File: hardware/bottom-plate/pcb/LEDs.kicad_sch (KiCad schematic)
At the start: 96 parts

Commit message: kicker pcb done, working on bottom plate
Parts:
- R100, R101, R102, R103, R104, R105, R106, R107, R108, R109, R110, R111, R112, R113, R114, R115, R68, R69, R70, R71, R72, R73, R74, R75, R76, R77, R78, R79, R80, R81, R82, R83, R84, R85, R86, R87, R88, R89, R90, R91, R92, R93, R94, R95, R96, R97, R98, R99: footprint PCM_Resistor_SMD_AKL:R_0603_1608Metric_Pad0.98x0.95mm_HandSolder -> PCM_Resistor_SMD_AKL:R_0805_2012Metric_Pad1.15x1.40mm_HandSolder

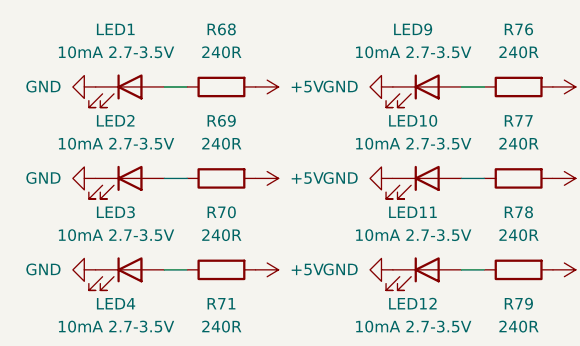
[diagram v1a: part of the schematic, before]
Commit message: cleaned up bottom plate schematic and added explanations of design decisions. Please read.
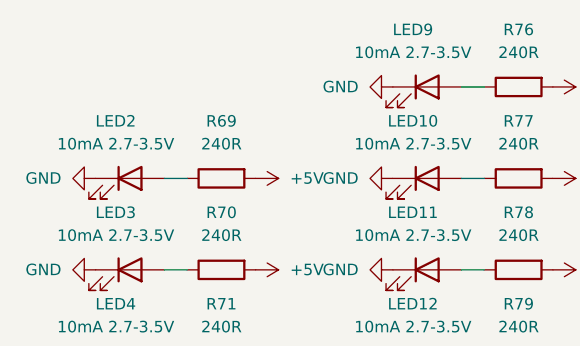
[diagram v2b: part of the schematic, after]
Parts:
- removed LED1: 10mA 2.7-3.5V, Diode_SMD:D_0603_1608Metric_Pad1.05x0.95mm_HandSolder, symbol Device:LED
- removed R68: 240R, PCM_Resistor_SMD_AKL:R_0805_2012Metric_Pad1.15x1.40mm_HandSolder, symbol Device:R
